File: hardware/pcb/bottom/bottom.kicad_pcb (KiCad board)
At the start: 2 copper layers, 65 x 120 mm, 38 parts, among them J1 Conn_01x15_Socket

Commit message: Optimize routing and improve grounding
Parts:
- added C10: 0.1uF, Bottom-Footprints:C_0805_2012Metric_Pad1.18x1.45mm_HandSolder, F.Cu at (172.9, 111.2)
- added C11: 0.1uF, Bottom-Footprints:C_0805_2012Metric_Pad1.18x1.45mm_HandSolder, F.Cu at (172.9, 133.2)
- added C2: 0.1uF, Bottom-Footprints:C_0805_2012Metric_Pad1.18x1.45mm_HandSolder, F.Cu at (131.9, 44.3)
- added C3: 0.1uF, Bottom-Footprints:C_0805_2012Metric_Pad1.18x1.45mm_HandSolder, F.Cu at (131.9, 66.6)
- added C4: 0.1uF, Bottom-Footprints:C_0805_2012Metric_Pad1.18x1.45mm_HandSolder, F.Cu at (131.9, 88.6)
- added C5: 0.1uF, Bottom-Footprints:C_0805_2012Metric_Pad1.18x1.45mm_HandSolder, F.Cu at (131.9, 111.1)
- added C6: 0.1uF, Bottom-Footprints:C_0805_2012Metric_Pad1.18x1.45mm_HandSolder, F.Cu at (132.1, 133.1)
- added C7: 0.1uF, Bottom-Footprints:C_0805_2012Metric_Pad1.18x1.45mm_HandSolder, F.Cu at (173.1, 44.1)
- added C8: 0.1uF, Bottom-Footprints:C_0805_2012Metric_Pad1.18x1.45mm_HandSolder, F.Cu at (172.9, 66.6)
- added C9: 0.1uF, Bottom-Footprints:C_0805_2012Metric_Pad1.18x1.45mm_HandSolder, F.Cu at (172.9, 88.7)
- C1: value 100nF -> 0.1uF
- R11, R12, R13, R14, R15, R16, R17, R18, R19, R20: value 470 -> 220
- moved R1 30.4 mm to (165.5, 73.5)
- moved R8 30.4 mm to (165.5, 43.1)
- moved R2 25.4 mm to (165.5, 71.0)
- moved R6 25.4 mm to (165.5, 45.6)
- moved R3 17.8 mm to (165.5, 68.5)
- moved R7 17.8 mm to (165.5, 50.8)
- moved R4 7.62 mm to (138.5, 40.6)
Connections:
- R11 pad 1: +3.3V -> VBAT
- R12 pad 1: +3.3V -> VBAT
- R13 pad 1: +3.3V -> VBAT
- R14 pad 1: +3.3V -> VBAT
- R15 pad 1: +3.3V -> VBAT
- R16 pad 1: +3.3V -> VBAT
- R17 pad 1: +3.3V -> VBAT
- R18 pad 1: +3.3V -> VBAT
- R19 pad 1: +3.3V -> VBAT
- R20 pad 1: +3.3V -> VBAT
- U1 pad 1: unconnected-(U1-VBAT-Pad1) -> VBAT
- U1 pad 15: ENC_DT -> ROW2
- U1 pad 16: ENC_CLK -> ROW1
- U1 pad 17: ENC_SW -> ROW0
- U1 pad 31: COL2 -> BT_SELECT
- U1 pad 32: COL1 -> COL0
- U1 pad 33: COL0 -> COL1
- U1 pad 34: BT_SELECT -> COL2
- U1 pad 5: ROW0 -> ENC_SW
- U1 pad 6: ROW1 -> ENC_CLK
- U1 pad 8: ROW2 -> ENC_DT
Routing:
- net VBAT: track 0.00 -> 312.3 mm
- net +3.3V: track 304.3 -> 182.4 mm, vias 9 -> 0
- net ROW0: track 122.5 -> 84.6 mm, vias 1 -> 0
- net ENC_SW: track 80.8 -> 115.8 mm
- net ROW1: track 119.7 -> 86.8 mm, vias 1 -> 0
- net ROW2: track 113.7 -> 89.1 mm, vias 1 -> 0
- net GND: track 22.3 -> 0.00 mm, vias 11 -> 163
- net ENC_CLK: track 93.0 -> 112.8 mm, vias 1 -> 0
- net ENC_DT: track 96.1 -> 107.4 mm, vias 1 -> 0
- net COL0: track 122.0 -> 111.3 mm
- net BT_SELECT: track 123.4 -> 113.7 mm
- net OLED_SCL: track 121.0 -> 111.7 mm, vias 2 -> 0
- net ROW3: track 111.4 -> 104.5 mm, vias 1 -> 0
- net COL1: track 120.4 -> 113.6 mm
- net COL2: track 119.5 -> 115.9 mm
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
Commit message: wip
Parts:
- C10, C11, C2, C3, C4, C5, C6, C7, C8, C9, R11, R12, R13, R14, R15, R16, R17, R18, R19, R20: moved to B.Cu
- D1, D10, D2, D3, D4, D5, D6, D7, D8, D9: footprint Bottom-Footprints:LED_SK6812MINI_PLCC4_3.5x3.5mm_P1.75mm -> Bottom-Footprints:SK6812-MINI-E; moved to B.Cu
- moved C7 1.27 mm to (171.9, 44.3)
- moved C5 1.26 mm to (133.1, 111.1)
- moved C2 1.01 mm to (132.9, 44.3)
- moved C3 1.01 mm to (132.9, 66.6)
- moved C4 1.01 mm to (132.9, 88.6)
- moved C6 1.00 mm to (133.1, 133.1)
- moved C8 1.00 mm to (171.9, 66.6)
- moved C10 0.88 mm to (172.0, 111.1)
- moved C11 0.88 mm to (172.0, 133.1)
- moved R11 0.87 mm to (130.4, 44.3)
- moved R12 0.87 mm to (130.4, 66.6)
- moved R13 0.87 mm to (130.4, 88.6)
- moved R14 0.87 mm to (130.6, 111.1)
- moved R15 0.87 mm to (130.6, 133.1)
- moved C9 0.86 mm to (172.0, 88.6)
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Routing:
- net VBAT: track 312.3 -> 278.1 mm
- net Net-(D10-DOUT): track 25.2 -> 29.3 mm, vias 0 -> 2
- net Net-(D7-DIN): track 25.1 -> 29.1 mm, vias 0 -> 2
- net Net-(D1-DOUT): track 25.1 -> 29.0 mm, vias 0 -> 2
- net Net-(D2-DOUT): track 25.1 -> 28.9 mm, vias 0 -> 2
- net Net-(D6-DIN): track 25.1 -> 28.8 mm, vias 0 -> 2
- net Net-(D8-DIN): track 25.1 -> 28.7 mm, vias 0 -> 2
- net Net-(D4-DOUT): track 25.1 -> 28.5 mm, vias 0 -> 2
- net Net-(D3-DOUT): track 25.1 -> 28.3 mm, vias 0 -> 2
- net RGB_LEDS: track 19.9 -> 18.8 mm, vias 1 -> 2
- net Net-(D10-DIN): track 78.8 -> 79.1 mm, vias 0 -> 2
- net GND: vias 163 -> 133

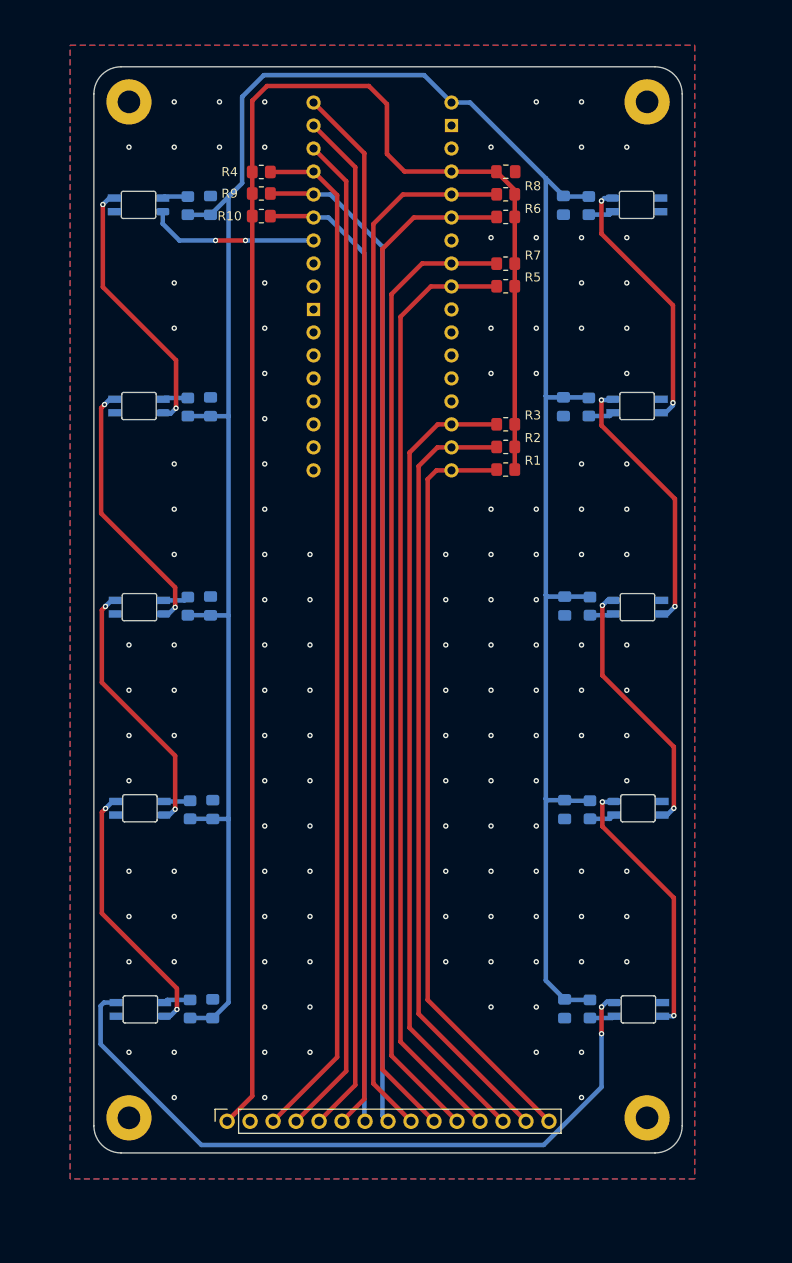
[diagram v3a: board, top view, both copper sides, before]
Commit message: Add SOT95P280X145-6N footprint to Bottom-Footprints library
- Created a new footprint for the SOT95P280X145-6N component.
- Included necessary pads, silkscreen, and fabrication lines.
- Added 3D model reference for TPS22918DBVR.
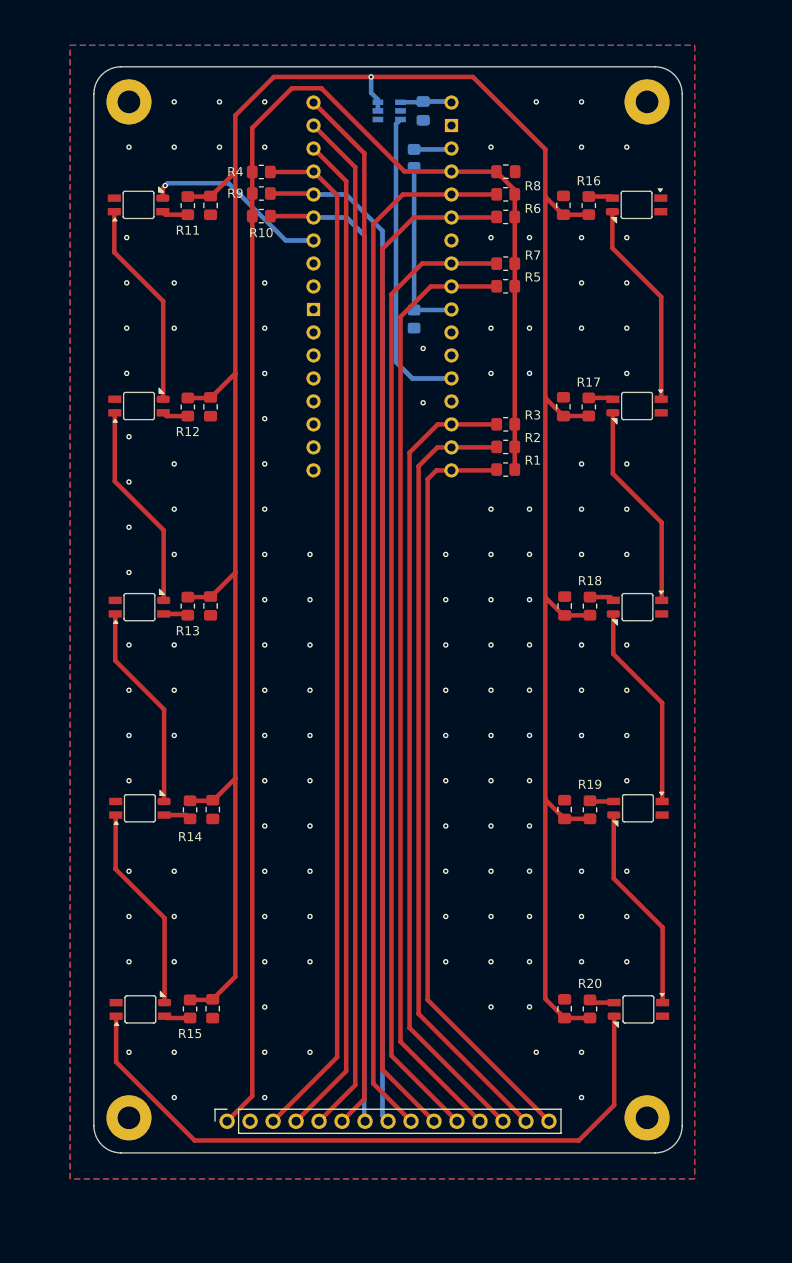
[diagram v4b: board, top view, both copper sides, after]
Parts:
- added C12: 0.1uF, Bottom-Footprints:C_0805_2012Metric_Pad1.18x1.45mm_HandSolder, B.Cu at (156.4, 33.9)
- added IC1: TPS22918DBVR, Bottom-Footprints:SOT95P280X145-6N, B.Cu at (152.6, 33.9)
- added R21: 10k, Bottom-Footprints:R_0805_2012Metric_Pad1.20x1.40mm_HandSolder, B.Cu at (155.4, 39.1)
- added R22: 10k, Bottom-Footprints:R_0805_2012Metric_Pad1.20x1.40mm_HandSolder, B.Cu at (155.4, 56.9)
- C10, C11, C2, C3, C4, C5, C6, C7, C8, C9, D1, D10, D2, D3, D4, D5, D6, D7, D8, D9, R11, R12, R13, R14, R15, R16, R17, R18, R19, R20: moved to F.Cu
- moved G*** 12.1 mm to (152.0, 136.1)
- turned C10 to -90 degrees
- turned C11 to -90 degrees
- turned C2 to 90 degrees
- turned C3 to 90 degrees
- turned C4 to 90 degrees
- turned C5 to 90 degrees
- turned C6 to 90 degrees
- turned C7 to -90 degrees
- turned C8 to -90 degrees
- turned C9 to -90 degrees
- turned R11 to -90 degrees
- turned R12 to -90 degrees
- turned R13 to -90 degrees
- turned R14 to -90 degrees
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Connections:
- C10 pad 2: VBAT -> LED_PWR
- C11 pad 2: VBAT -> LED_PWR
- C2 pad 2: VBAT -> LED_PWR
- C3 pad 2: VBAT -> LED_PWR
- C4 pad 2: VBAT -> LED_PWR
- C5 pad 2: VBAT -> LED_PWR
- C6 pad 2: VBAT -> LED_PWR
- C7 pad 2: VBAT -> LED_PWR
- C8 pad 2: VBAT -> LED_PWR
- C9 pad 2: VBAT -> LED_PWR
- R11 pad 1: VBAT -> LED_PWR
- R12 pad 1: VBAT -> LED_PWR
- R13 pad 1: VBAT -> LED_PWR
- R14 pad 1: VBAT -> LED_PWR
- R15 pad 1: VBAT -> LED_PWR
- R16 pad 1: VBAT -> LED_PWR
- R17 pad 1: VBAT -> LED_PWR
- R18 pad 1: VBAT -> LED_PWR
- R19 pad 1: VBAT -> LED_PWR
- R20 pad 1: VBAT -> LED_PWR
- U1 pad 10: unconnected-(U1-21-Pad10) -> VBUS_SENSE
- U1 pad 13: unconnected-(U1-16-Pad13) -> LED_STATUS
- U1 pad 2: unconnected-(U1-GND-Pad2) -> GND
- U1 pad 3: unconnected-(U1-5V-Pad3) -> +5V
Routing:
- net LED_PWR: track 0.00 -> 291.3 mm, vias 0 -> 1
- net VBAT: track 278.1 -> 5.43 mm
- net LED_STATUS: track 0.00 -> 33.9 mm
- net VBUS_SENSE: track 0.00 -> 19.9 mm
- net Net-(D10-DOUT): track 29.3 -> 23.0 mm, vias 2 -> 0
- net Net-(D7-DIN): track 29.1 -> 23.0 mm, vias 2 -> 0
- net Net-(D1-DOUT): track 29.0 -> 23.0 mm, vias 2 -> 0
- net Net-(D2-DOUT): track 28.9 -> 23.0 mm, vias 2 -> 0
- net Net-(D6-DIN): track 28.8 -> 23.0 mm, vias 2 -> 0
- net Net-(D8-DIN): track 28.7 -> 23.0 mm, vias 2 -> 0
- net Net-(D4-DOUT): track 28.5 -> 23.0 mm, vias 2 -> 0
- net Net-(D3-DOUT): track 28.3 -> 23.0 mm, vias 2 -> 0
- net +3.3V: track 182.4 -> 177.2 mm
- net +5V: track 0.00 -> 4.17 mm
- net Net-(D10-DIN): track 79.1 -> 75.1 mm, vias 2 -> 0
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
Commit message: changed m2.5 mh to m2, added screws and nuts to enclosure.FCStd
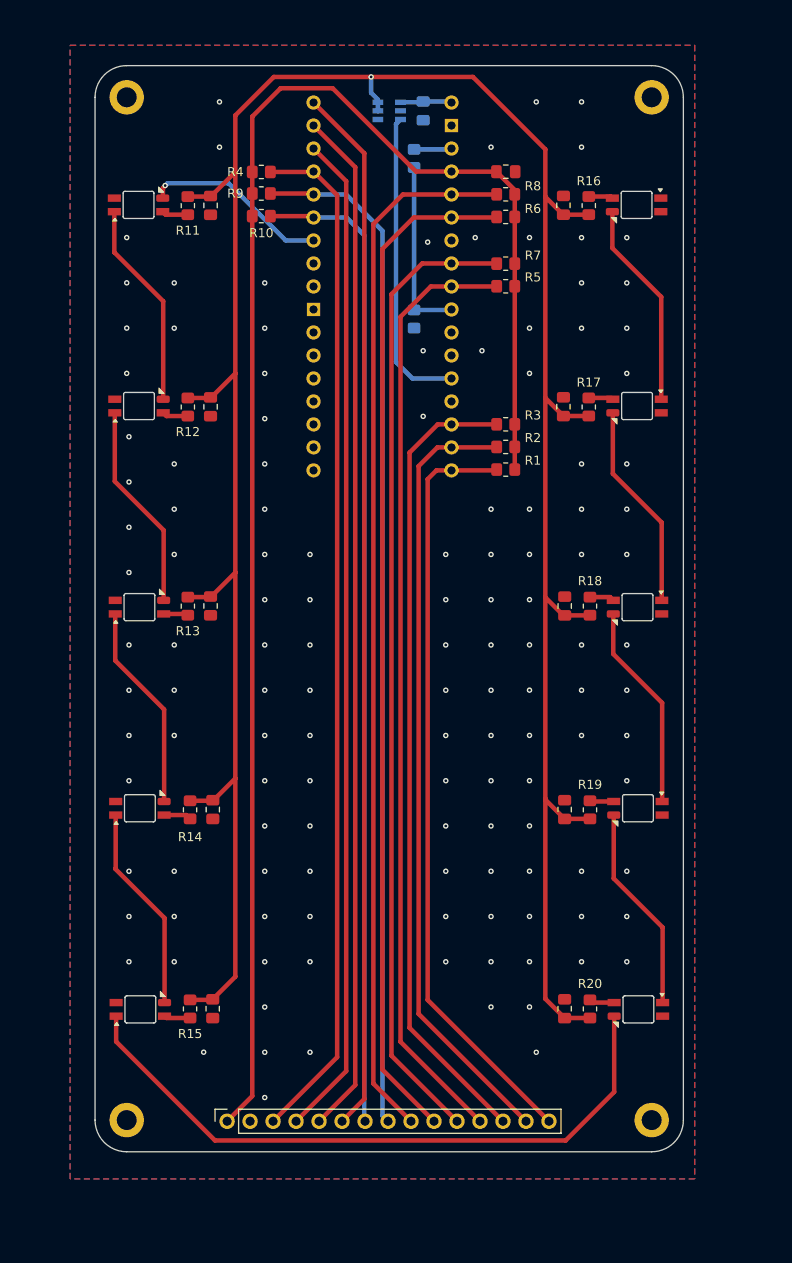
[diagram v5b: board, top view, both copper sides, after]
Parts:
- H1, H2, H3, H4: footprint Bottom-Footprints:MountingHole_2.5mm_Pad -> MountingHole:MountingHole_2.2mm_M2_DIN965_Pad
- moved H2 0.72 mm to (181.6, 32.4)
- moved H1 0.57 mm to (123.6, 32.4)
- moved H3 0.57 mm to (181.6, 145.4)
- moved H4 0.35 mm to (123.6, 145.4)
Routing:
- net Net-(D10-DIN): track 75.1 -> 73.0 mm
- net +3.3V: track 177.2 -> 178.0 mm
- net GND: vias 142 -> 131
- net (no net): vias 0 -> 1
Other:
- outline, holes or cut-outs redrawn
